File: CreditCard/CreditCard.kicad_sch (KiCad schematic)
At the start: 9 parts

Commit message: début
début sch
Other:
- added sheet MCU (MCU.kicad_sch)
- added sheet PWR (PWR.kicad_sch)
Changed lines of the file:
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@@
 (kicad_sch
-	(version 20231120)
+	(version 20250114)
 	(generator "eeschema")
-	(generator_version "8.0")
+	(generator_version "9.0")
 	(paper "A4")
+	(rectangle
+		(start 146.05 12.7)
+		(end 214.63 74.676)
+		(stroke
+			(width 0.381)
+			(type dash)
+			(color 20 0 0 1)
+		)
+		(fill
+			(type none)
+		)
+	)
+	(rectangle
+		(start 215.9 12.7)
+		(end 284.48 74.676)
+		(stroke
+			(width 0.381)
+			(type dash)
+			(color 20 0 0 1)
+		)
+		(fill
+			(type none)
+		)
+	)
+	(text "Équipe #10 - C3i\nPCB Carte de crédit\nA25"
+		(exclude_from_sim no)
+		(at 14.478 42.926 0)
+		(effects
+			(font
+				(face "Calibri")
+				(size 11.43 11.43)
+				(thickness 0.254)
+				(bold yes)
+			)
+			(justify left)
+		)
+	)
+	(text "BOTTOM\n"
+		(exclude_from_sim no)
+		(at 262.636 37.084 0)
+		(effects
+			(font
+				(size 2.286 2.286)
+				(thickness 0.4064)
+				(bold yes)
+			)
+		)
+	)
+	(text "TESTPOINTS"
+		(exclude_from_sim no)
+		(at 157.734 16.002 0)
+		(effects
+			(font
+				(size 2.286 2.286)
+				(thickness 0.4064)
+				(bold yes)
+			)
+		)
+	)
+	(text "FIDUCIALS\n"
+		(exclude_from_sim no)
+		(at 225.552 16.002 0)
+		(effects
+			(font
+				(size 2.286 2.286)
+				(thickness 0.4064)
+				(bold yes)
+			)
+		)
+	)
+	(text "TOP"
+		(exclude_from_sim no)
+		(at 236.474 37.592 0)
+		(effects
+			(font
+				(size 2.286 2.286)
+				(thickness 0.4064)
+				(bold yes)
+			)
+		)
+	)
 	(wire
 		(pts
@@
 		)
 	)
-	(rectangle
-		(start 146.05 12.7)
-		(end 214.63 74.676)
-		(stroke
-			(width 0.381)
-			(type dash)
-			(color 20 0 0 1)
-		)
-		(fill
-			(type none)
-		)
-	)
-	(rectangle
-		(start 215.9 12.7)
-		(end 284.48 74.676)
-		(stroke
-			(width 0.381)
-			(type dash)
-			(color 20 0 0 1)
-		)
-		(fill
-			(type none)
-		)
-	)
 	(image
 		(at 249.428 114.3)
@@
 		)
 	)
-	(text "Équipe #10 - C3i\nPCB Carte de crédit\nA25"
-		(exclude_from_sim no)
-		(at 14.478 42.926 0)
-		(effects
-			(font
-				(face "Calibri")
-				(size 11.43 11.43)
-				(thickness 0.254)
-				(bold yes)
-			)
-			(justify left)
-		)
-	)
-	(text "BOTTOM\n"
-		(exclude_from_sim no)
-		(at 262.636 37.084 0)
-		(effects
-			(font
-				(size 2.286 2.286)
-				(thickness 0.4064)
-				(bold yes)
-			)
-		)
-	)
-	(text "TESTPOINTS"
-		(exclude_from_sim no)
-		(at 157.734 16.002 0)
-		(effects
-			(font
-				(size 2.286 2.286)
-				(thickness 0.4064)
-				(bold yes)
-			)
-		)
-	)
-	(text "FIDUCIALS\n"
-		(exclude_from_sim no)
-		(at 225.552 16.002 0)
-		(effects
-			(font
-				(size 2.286 2.286)
-				(thickness 0.4064)
-				(bold yes)
-			)
-		)
-	)
-	(text "TOP"
-		(exclude_from_sim no)
-		(at 236.474 37.592 0)
-		(effects
-			(font
-				(size 2.286 2.286)
-				(thickness 0.4064)
-				(bold yes)
-			)
-		)
-	)
 	(symbol
 		(lib_id "LIB:Fiducial")
@@
 		(at 24.13 144.78)
 		(size 69.85 39.37)
+		(exclude_from_sim no)
+		(in_bom yes)
+		(on_board yes)
+		(dnp no)
 		(fields_autoplaced yes)
 		(stroke
@@
 		)
 	)
+	(sheet
+		(at 22.86 111.76)
+		(size 71.12 30.48)
+		(exclude_from_sim no)
+		(in_bom yes)
+		(on_board yes)
+		(dnp no)
+		(fields_autoplaced yes)
+		(stroke
+			(width 0.1524)
+			(type solid)
+		)
+		(fill
+			(color 0 0 0 0.0000)
+		)
+		(property "Sheetname" "PWR"
+			(at 22.86 111.0484 0)
+			(effects
+				(font
+					(size 1.27 1.27)
+				)
+				(justify left bottom)
+			)
+		)
+		(property "Sheetfile" "PWR.kicad_sch"
+			(at 22.86 142.8246 0)
+			(effects
+				(font
+					(size 1.27 1.27)
+				)
+				(justify left top)
+			)
+		)
+		(instances
+			(project "CreditCard"
+				(path "/374dba13-75d6-44a0-b8b2-0ca0aa70330e"
+					(page "4")
+				)
+			)
+		)
+	)
+	(sheet
+		(at 96.52 144.78)
+		(size 78.74 38.1)
+		(exclude_from_sim no)
+		(in_bom yes)
+		(on_board yes)
+		(dnp no)
+		(fields_autoplaced yes)
+		(stroke
+			(width 0.1524)
+			(type solid)
+		)
+		(fill
+			(color 0 0 0 0.0000)
+		)
+		(property "Sheetname" "MCU"
+			(at 96.52 144.0684 0)
+			(effects
+				(font
+					(size 1.27 1.27)
+				)
+				(justify left bottom)
+			)
+		)
+		(property "Sheetfile" "MCU.kicad_sch"
+			(at 96.52 183.4646 0)
+			(effects
+				(font
+					(size 1.27 1.27)
+				)
+				(justify left top)
+			)
+		)
+		(instances
+			(project "CreditCard"
+				(path "/374dba13-75d6-44a0-b8b2-0ca0aa70330e"
+					(page "3")
+				)
+			)
+		)
+	)
 	(sheet_instances
 		(path "/"
@@
 		)
 	)
+	(embedded_fonts no)
 )

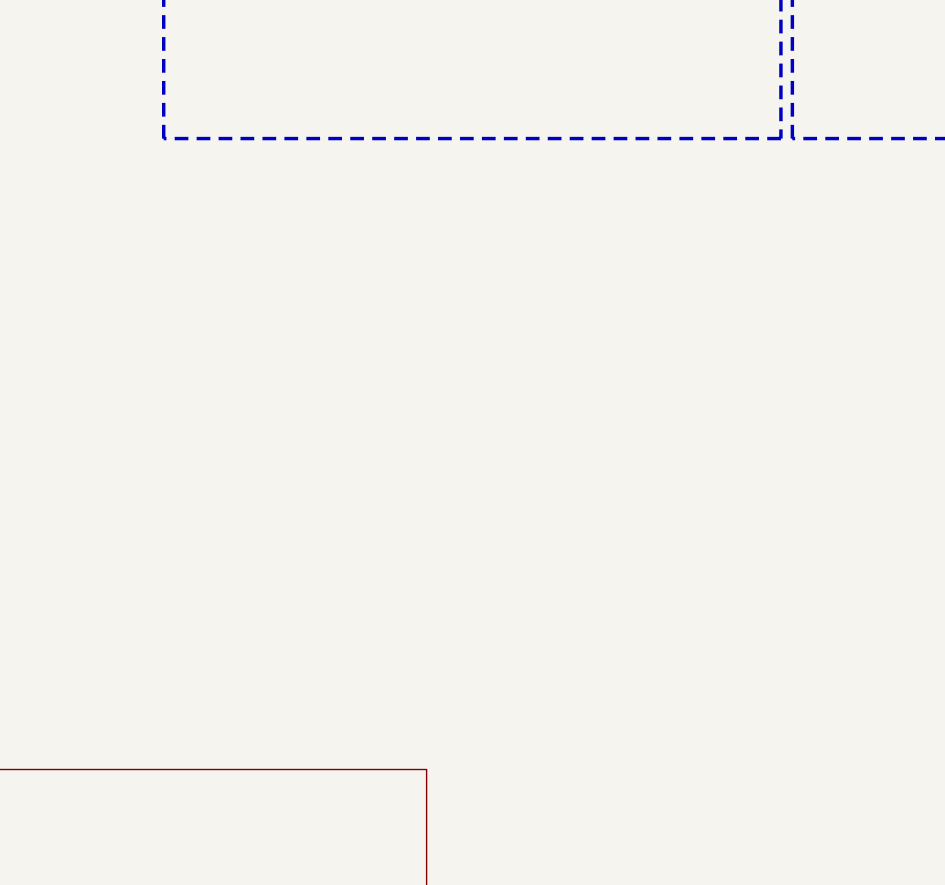
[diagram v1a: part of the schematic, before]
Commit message: ajout du LCD
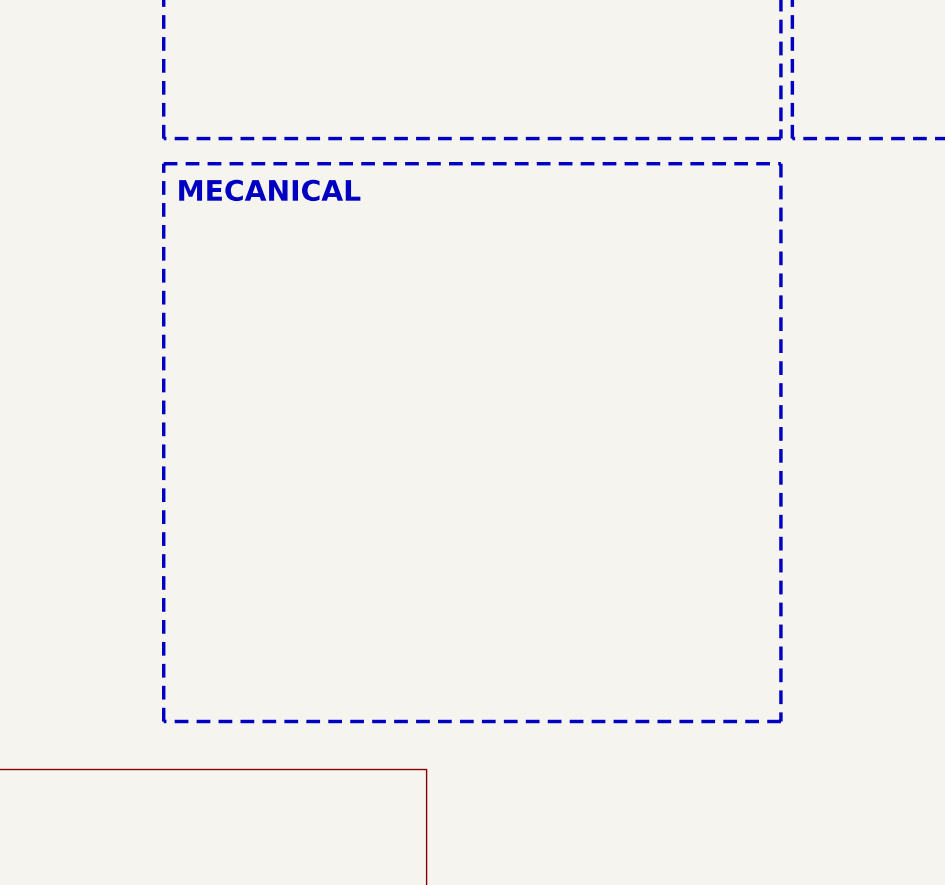
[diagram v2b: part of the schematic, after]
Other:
- note added: "MECANICAL"
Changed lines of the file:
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@@
+	)
+	(rectangle
+		(start 146.05 77.47)
+		(end 214.63 139.446)
+		(stroke
+			(width 0.381)
+			(type dash)
+			(color 20 0 0 1)
+		)
+		(fill
+			(type none)
+		)
 	)
 	(rectangle
@@
 		(effects
 			(font
+				(size 2.286 2.286)
+				(thickness 0.4064)
+				(bold yes)
+			)
+		)
+	)
+	(text "MECANICAL\n"
+		(exclude_from_sim no)
+		(at 157.734 80.772 0)
+		(effects
+			(font

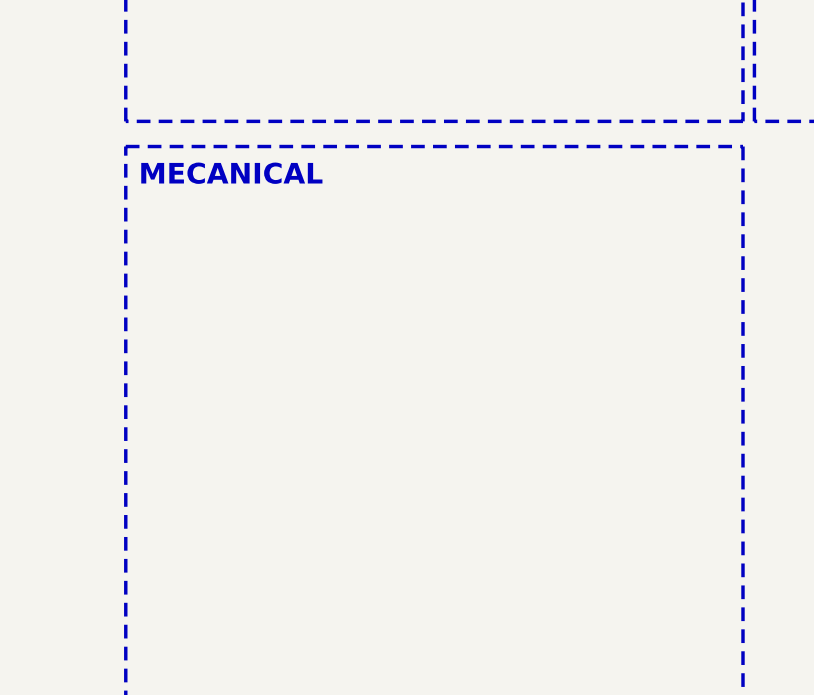
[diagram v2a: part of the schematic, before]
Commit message: ajout des mounting holes 3mm
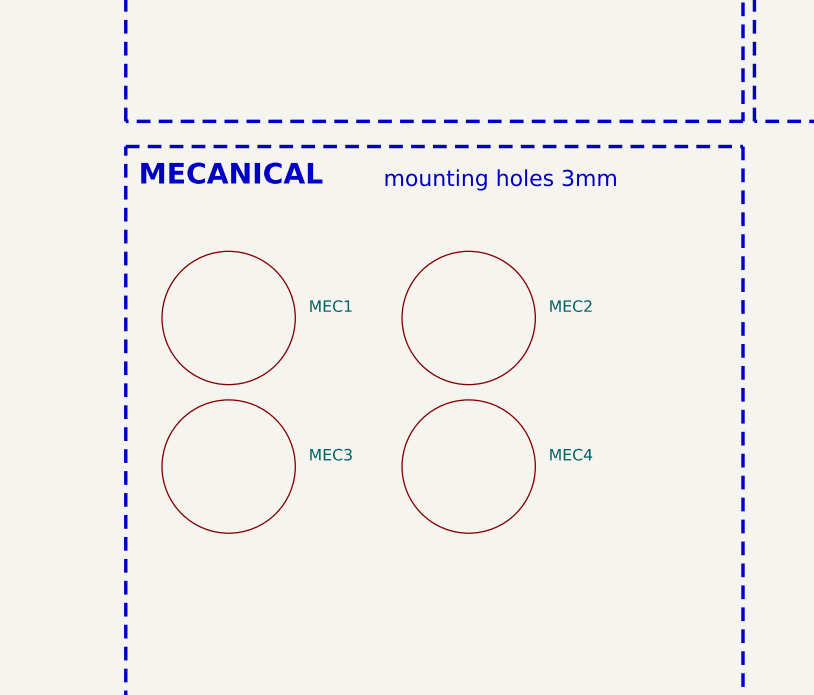
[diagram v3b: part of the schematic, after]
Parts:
- added MEC1, MEC2, MEC3, MEC4: ~, Library:Mounting_3mm, symbol Library:mounting_3mm
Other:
- note added: "mounting holes 3mm"

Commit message: gerber crée
pcb terminer
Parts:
- removed TP1: TestPoint, TestPoint:TestPoint_Pad_D1.5mm, symbol Connector:TestPoint
- added Vbat_TP1, Vbus_TP1, Vsys_TP1: TP, TestPoint:TestPoint_Pad_D1.5mm, symbol Connector:TestPoint
- renumbered 3VTP1 to 3V3_TP1, GNDTP1 to GND_TP1
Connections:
- new net Vbat: Vbat_TP1.1
- new net Vbus: Vbus_TP1.1
- new net Vsys: Vsys_TP1.1
